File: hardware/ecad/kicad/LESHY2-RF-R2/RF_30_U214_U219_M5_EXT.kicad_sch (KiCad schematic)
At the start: 52 parts, among them J10 Samtec HLE-107-02-G-DV-PE-LC, J11 1125R-SMT-4P, U86 Texas Instruments TPD4E05U06D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, U87 Texas Instruments TPD4E05U06D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, U88 Texas Instruments TPD4E05U06D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, U89 Nexperia 74LVC126APW,118, U90 Nexperia 74LVC126APW,118, U91 TCA4307DGKR, U92 Nexperia 74LVC126APW,118, U93 TPS3808G33DBVR, U94 Texas Instruments TPS259470LR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, U95 Texas Instruments TPD4E05U06D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, U96 Texas Instruments TXS0102DCUR, U97 TPS3808G33DBVR

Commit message: Verify factory-placeable Airband filter
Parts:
- renumbered C236 to C235, C237 to C236, C238 to C237, C239 to C238, C240 to C239, C241 to C240, C242 to C241, C243 to C242, C244 to C243, C245 to C244, C246 to C245, C247 to C246, C248 to C247, C249 to C248
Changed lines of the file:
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@@
 		(on_board yes)
 		(dnp no)
-		(property "Reference" "C236"
+		(property "Reference" "C235"
 			(at 55.88 44.45 0)
 			(show_name no)
@@
 			(project "LESHY2-RF-R2"
 				(path "/ae77990d-9208-5dc0-8562-26b7a6671c82"
-					(reference "C236")
+					(reference "C235")
 					(unit 1)
 				)
@@
 		(on_board yes)
 		(dnp no)
-		(property "Reference" "C237"
+		(property "Reference" "C236"
 			(at 147.32 44.45 0)
 			(show_name no)
@@
 			(project "LESHY2-RF-R2"
 				(path "/ae77990d-9208-5dc0-8562-26b7a6671c82"
-					(reference "C237")
+					(reference "C236")
 					(unit 1)
 				)
@@
 		(on_board yes)
 		(dnp no)
-		(property "Reference" "C238"
+		(property "Reference" "C237"
 			(at 238.76 44.45 0)
 			(show_name no)
@@
 			(project "LESHY2-RF-R2"
 				(path "/ae77990d-9208-5dc0-8562-26b7a6671c82"
-					(reference "C238")
+					(reference "C237")
 					(unit 1)
 				)
@@
 		(on_board yes)
 		(dnp no)
-		(property "Reference" "C239"
+		(property "Reference" "C238"
 			(at 330.20 44.45 0)
 			(show_name no)
@@
 			(project "LESHY2-RF-R2"
 				(path "/ae77990d-9208-5dc0-8562-26b7a6671c82"
-					(reference "C239")
+					(reference "C238")
 					(unit 1)
 				)
@@
 		(on_board yes)
 		(dnp no)
-		(property "Reference" "C240"
+		(property "Reference" "C239"
 			(at 421.64 44.45 0)
 			(show_name no)
@@
 			(project "LESHY2-RF-R2"
 				(path "/ae77990d-9208-5dc0-8562-26b7a6671c82"
-					(reference "C240")
+					(reference "C239")
 					(unit 1)
 				)
@@
 		(on_board yes)
 		(dnp no)
-		(property "Reference" "C241"
+		(property "Reference" "C240"
 			(at 513.08 44.45 0)
 			(show_name no)
@@
 			(project "LESHY2-RF-R2"
 				(path "/ae77990d-9208-5dc0-8562-26b7a6671c82"
-					(reference "C241")
+					(reference "C240")
 					(unit 1)
 				)
@@
 		(on_board yes)
 		(dnp no)
-		(property "Reference" "C242"
+		(property "Reference" "C241"
 			(at 604.52 44.45 0)
 			(show_name no)
@@
 			(project "LESHY2-RF-R2"
 				(path "/ae77990d-9208-5dc0-8562-26b7a6671c82"
-					(reference "C242")
+					(reference "C241")
 					(unit 1)
 				)
@@
 		(on_board yes)
 		(dnp no)
-		(property "Reference" "C243"
+		(property "Reference" "C242"
 			(at 695.96 44.45 0)
 			(show_name no)
@@
 			(project "LESHY2-RF-R2"
 				(path "/ae77990d-9208-5dc0-8562-26b7a6671c82"
-					(reference "C243")
+					(reference "C242")
 					(unit 1)
 				)
@@
 		(on_board yes)
 		(dnp no)
-		(property "Reference" "C244"
+		(property "Reference" "C243"
 			(at 787.40 44.45 0)
 			(show_name no)
@@
 			(project "LESHY2-RF-R2"
 				(path "/ae77990d-9208-5dc0-8562-26b7a6671c82"
-					(reference "C244")
+					(reference "C243")
 					(unit 1)
 				)
@@
 		(on_board yes)
 		(dnp no)
-		(property "Reference" "C245"
+		(property "Reference" "C244"
 			(at 878.84 44.45 0)
 			(show_name no)
@@
 			(project "LESHY2-RF-R2"
 				(path "/ae77990d-9208-5dc0-8562-26b7a6671c82"
-					(reference "C245")
+					(reference "C244")
 					(unit 1)
 				)
@@
 		(on_board yes)
 		(dnp no)
-		(property "Reference" "C246"
+		(property "Reference" "C245"
 			(at 970.28 44.45 0)
 			(show_name no)
@@
 			(project "LESHY2-RF-R2"
 				(path "/ae77990d-9208-5dc0-8562-26b7a6671c82"
-					(reference "C246")
+					(reference "C245")
 					(unit 1)
 				)
@@
 		(on_board yes)
 		(dnp no)
-		(property "Reference" "C247"
+		(property "Reference" "C246"
 			(at 1061.72 44.45 0)
 			(show_name no)
@@
 			(project "LESHY2-RF-R2"
 				(path "/ae77990d-9208-5dc0-8562-26b7a6671c82"
-					(reference "C247")
+					(reference "C246")
 					(unit 1)
 				)
@@
 		(on_board yes)
 		(dnp no)
-		(property "Reference" "C248"
+		(property "Reference" "C247"
 			(at 55.88 80.01 0)
 			(show_name no)
@@
 			(project "LESHY2-RF-R2"
 				(path "/ae77990d-9208-5dc0-8562-26b7a6671c82"
-					(reference "C248")
+					(reference "C247")
 					(unit 1)
 				)
@@
 		(on_board yes)
 		(dnp no)
-		(property "Reference" "C249"
+		(property "Reference" "C248"
 			(at 147.32 80.01 0)
 			(show_name no)
@@
 			(project "LESHY2-RF-R2"
 				(path "/ae77990d-9208-5dc0-8562-26b7a6671c82"
-					(reference "C249")
-					(unit 1)
-				)
+					(reference "C248")
+					(unit 1)
+				)

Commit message: Complete current R2 schematic and sourcing revalidation
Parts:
- removed R214: Panasonic ERJ-2RKF22R0X, Resistor_SMD:R_0402_1005Metric, symbol Leshy2_R2:panasonic_erj_2rkf22r0x
- added C246, C248, C249: Yageo CC0402KRX7R9BB104, Capacitor_SMD:C_0402_1005Metric, symbol Leshy2_R2:yageo_cc0402krx7r9bb104
- added C247: Murata GRM155R71H103KA88D, Capacitor_SMD:C_0402_1005Metric, symbol Leshy2_R2:murata_grm155r71h103ka88d
- added L32: LESHY2-NFC-PICKUP-LOOP-R2, Leshy2_R2:NFC_Pickup_Loop_R2, symbol Leshy2_R2:leshy2_nfc_pickup_loop_r2
- added R226, R232: 0402WGF1003TCE, Resistor_SMD:R_0402_1005Metric, symbol Leshy2_R2:uniroyal_0402wgf1003tce
- added R227: 0402WGF1004TCE, Resistor_SMD:R_0402_1005Metric, symbol Leshy2_R2:uniroyal_0402wgf1004tce
- added R228, R229: 0402WGF1001TCE, Resistor_SMD:R_0402_1005Metric, symbol Leshy2_R2:uniroyal_0402wgf1001tce
- added R230, R231, R233, R234: 0402WGF1002TCE, Resistor_SMD:R_0402_1005Metric, symbol Leshy2_R2:uniroyal_0402wgf1002tce
- added U95, U96: BAT54S,215, Package_TO_SOT_SMD:SOT-23, symbol Leshy2_R2:nexperia_bat54s_215
- added U97: LMV331IDBVR, Package_TO_SOT_SMD:SOT-23-5, symbol Leshy2_R2:ti_lmv331_idbvr
- added U98: Texas Instruments SN74LVC1G06DCKR, Package_TO_SOT_SMD:Texas_R-PDSO-G5_DCK-5, symbol Leshy2_R2:ti_sn74lvc1g06_dckr
- added U99: SN74CBTLV1G125DCKR, Package_TO_SOT_SMD:Texas_R-PDSO-G5_DCK-5, symbol Leshy2_R2:ti_sn74cbtlv1g125_dckr
- renumbered C235 to C240, C236 to C241, C237 to C242, C238 to C243, C239 to C244, C240 to C245, C241 to C250, C242 to C251, C243 to C252, C244 to C253, C245 to C254, C246 to C255, C247 to C256, C248 to C257, R211 to R212, R212 to R213, R213 to R214, R226 to R235, R227 to R236, R228 to R237, R229 to R238, R230 to R239, R231 to R240, R232 to R241, R233 to R242, R234 to R243, U94 to U100, U95 to U101, U96 to U102, U97 to U103, U86 to U87, U87 to U88, U88 to U89, U89 to U90, U90 to U91, U91 to U92, U92 to U93, U93 to U94
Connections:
- net 3V3_MAIN: now also C249.1 (END_1), U99.5 (VCC)
- net AON_SAFE_3V3: now also C246.1 (END_1), C248.1 (END_1), R230.1 (END_1), R232.1 (END_1), R234.1 (END_1), U97.5 (VCC), U98.5 (VCC)
- net POWER_GROUND: now also U93.1 (1OE), U93.2 (1A), C249.2 (END_2), U99.3 (GND)
- net SAFETY_GROUND: now also C246.2 (END_2), C247.2 (END_2), C248.2 (END_2), R226.2 (END_2), R231.2 (END_2), R233.2 (END_2), U95.1 (A1), U96.1 (A1), U97.2 (GND), U98.3 (GND)
- net U214_BUSY_CONNECTOR: now also U99.2 (A); no longer U93.2 (1A)
- net U214_READY: now also R233.1 (END_1), U98.2 (A); no longer U93.1 (1OE)
- net U214_BUSY_BUFFERED: no longer names the net of U93.3 (1Y)
- new net CAP_PIN10_HOST: U99.4 (B)
- new net EV_N9_U219_NFC: R227.1 (END_1), R230.2 (END_2), U97.4 (OUT)
- new net NFC_BRIDGE_AC_N: R228.2 (END_2), U96.3 (K1_A2)
- new net NFC_BRIDGE_AC_P: R229.2 (END_2), U95.3 (K1_A2)
- new net NFC_FIELD_ENV: C247.1 (END_1), R226.1 (END_1), U95.2 (K2), U96.2 (K2), U97.3 (IN_N)
- new net NFC_FIELD_THRESHOLD: R227.2 (END_2), R231.1 (END_1), R232.2 (END_2), U97.1 (IN_P)
- new net NFC_PICKUP_N: L32.2 (END_N), R228.1 (END_1)
- new net NFC_PICKUP_P: L32.1 (END_P), R229.1 (END_1)
- new net U219_PIN10_OE_N: R234.2 (END_2), U98.4 (Y), U99.1 (OE_N)
- no-connect marks 22 -> 24
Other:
- moved on the sheet: C250, C251, C252, C253, C254, C255, C256, C257, J10, J11, R212, R213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

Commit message: Canonicalize physical ground anchors
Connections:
- net SAFETY_GROUND is gone; now on net POWER_GROUND: C244.2 (END_2), C245.2 (END_2), C246.2 (END_2), C247.2 (END_2), C248.2 (END_2), C256.2 (END_2), C257.2 (END_2), R224.2 (END_2), R226.2 (END_2), R231.2 (END_2), R233.2 (END_2), R242.2 (END_2), U103.2 (GND), U94.2 (GND), U95.1 (A1), U96.1 (A1), U97.2 (GND), U98.3 (GND)
- net U214_ESD_GROUND is gone; now on net POWER_GROUND: U87.3 (GND_3), U87.8 (GND_8), U88.3 (GND_3), U88.8 (GND_8), U89.3 (GND_3), U89.8 (GND_8)
- net U214_UNUSED_A_LOW is gone; now on net POWER_GROUND: U91.12 (4A), U91.5 (2A), U91.9 (3A)
- net U214_UNUSED_OE_LOW is gone; now on net POWER_GROUND: U91.10 (3OE), U91.13 (4OE), U91.4 (2OE)
- net UNIT_ESD_GROUND is gone; now on net POWER_GROUND: U101.3 (GND_3), U101.8 (GND_8)
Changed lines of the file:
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@@
 		(effects (font (size 1.27 1.27)))
 	)
-	(hierarchical_label "SAFETY_GROUND"
-		(shape bidirectional)
+	(label "POWER_GROUND"
 		(at 441.96 50.80 180)
 		(effects (font (size 1.27 1.27)) (justify right bottom))
@@
 		(effects (font (size 1.27 1.27)))
 	)
-	(label "SAFETY_GROUND"
+	(label "POWER_GROUND"
 		(at 533.40 50.80 180)
 		(effects (font (size 1.27 1.27)) (justify right bottom))
@@
 		(effects (font (size 1.27 1.27)))
 	)
-	(label "SAFETY_GROUND"
+	(label "POWER_GROUND"
 		(at 624.84 50.80 180)
 		(effects (font (size 1.27 1.27)) (justify right bottom))
@@
 		(effects (font (size 1.27 1.27)))
 	)
-	(label "SAFETY_GROUND"
+	(label "POWER_GROUND"
 		(at 716.28 50.80 180)
 		(effects (font (size 1.27 1.27)) (justify right bottom))
@@
 		(effects (font (size 1.27 1.27)))
 	)
-	(label "SAFETY_GROUND"
+	(label "POWER_GROUND"
 		(at 807.72 50.80 180)
 		(effects (font (size 1.27 1.27)) (justify right bottom))
@@
 		(effects (font (size 1.27 1.27)))
 	)
-	(label "SAFETY_GROUND"
+	(label "POWER_GROUND"
 		(at 441.96 86.36 180)
 		(effects (font (size 1.27 1.27)) (justify right bottom))
@@
 		(effects (font (size 1.27 1.27)))
 	)
-	(label "SAFETY_GROUND"
+	(label "POWER_GROUND"
 		(at 533.40 86.36 180)
 		(effects (font (size 1.27 1.27)) (justify right bottom))
@@
 		(effects (font (size 1.27 1.27)))
 	)
-	(label "SAFETY_GROUND"
+	(label "POWER_GROUND"
 		(at 990.60 121.92 180)
 		(effects (font (size 1.27 1.27)) (justify right bottom))
@@
 		(effects (font (size 1.27 1.27)))
 	)
-	(label "SAFETY_GROUND"
+	(label "POWER_GROUND"
 		(at 624.84 129.54 180)
 		(effects (font (size 1.27 1.27)) (justify right bottom))
@@
 		(effects (font (size 1.27 1.27)))
 	)
-	(label "SAFETY_GROUND"
+	(label "POWER_GROUND"
 		(at 441.96 157.48 180)
 		(effects (font (size 1.27 1.27)) (justify right bottom))
@@
 		(effects (font (size 1.27 1.27)))
 	)
-	(label "SAFETY_GROUND"
+	(label "POWER_GROUND"
 		(at 716.28 157.48 180)
 		(effects (font (size 1.27 1.27)) (justify right bottom))
@@
 		(effects (font (size 1.27 1.27)))
 	)
-	(label "SAFETY_GROUND"
+	(label "POWER_GROUND"
 		(at 350.52 193.04 180)
 		(effects (font (size 1.27 1.27)) (justify right bottom))
@@
 		(effects (font (size 1.27 1.27)))
 	)
-	(label "U214_ESD_GROUND"
+	(label "POWER_GROUND"
 		(at 492.76 195.58 0)
 		(effects (font (size 1.27 1.27)))
@@
 	(no_connect (at 533.40 193.04)
 	)
-	(label "U214_ESD_GROUND"
+	(label "POWER_GROUND"
 		(at 533.40 195.58 180)
 		(effects (font (size 1.27 1.27)) (justify right bottom))
@@
 		(effects (font (size 1.27 1.27)))
 	)
-	(label "U214_ESD_GROUND"
+	(label "POWER_GROUND"
 		(at 675.64 195.58 0)
 		(effects (font (size 1.27 1.27)))
@@
 	(no_connect (at 716.28 193.04)
 	)
-	(label "U214_ESD_GROUND"
+	(label "POWER_GROUND"
 		(at 716.28 195.58 180)
 		(effects (font (size 1.27 1.27)) (justify right bottom))
@@
 		(effects (font (size 1.27 1.27)))
 	)
-	(label "U214_ESD_GROUND"
+	(label "POWER_GROUND"
 		(at 767.08 195.58 0)
 		(effects (font (size 1.27 1.27)))
@@
 	(no_connect (at 807.72 193.04)
 	)
-	(label "U214_ESD_GROUND"
+	(label "POWER_GROUND"
 		(at 807.72 195.58 180)
 		(effects (font (size 1.27 1.27)) (justify right bottom))
@@
 		(effects (font (size 1.27 1.27)))
 	)
-	(label "U214_UNUSED_OE_LOW"
+	(label "POWER_GROUND"
 		(at 949.96 198.12 0)
 		(effects (font (size 1.27 1.27)))
 	)
-	(label "U214_UNUSED_A_LOW"
+	(label "POWER_GROUND"
 		(at 949.96 200.66 0)
 		(effects (font (size 1.27 1.27)))
@@
 	(no_connect (at 990.60 190.50)
 	)
-	(label "U214_UNUSED_A_LOW"
+	(label "POWER_GROUND"
 		(at 990.60 193.04 180)
 		(effects (font (size 1.27 1.27)) (justify right bottom))
 	)
-	(label "U214_UNUSED_OE_LOW"
+	(label "POWER_GROUND"
 		(at 990.60 195.58 180)
 		(effects (font (size 1.27 1.27)) (justify right bottom))
@@
 	(no_connect (at 990.60 198.12)
 	)
-	(label "U214_UNUSED_A_LOW"
+	(label "POWER_GROUND"
 		(at 990.60 200.66 180)
 		(effects (font (size 1.27 1.27)) (justify right bottom))
 	)
-	(label "U214_UNUSED_OE_LOW"
+	(label "POWER_GROUND"
 		(at 990.60 203.20 180)
 		(effects (font (size 1.27 1.27)) (justify right bottom))
@@
 		(effects (font (size 1.27 1.27)))
 	)
-	(label "SAFETY_GROUND"
+	(label "POWER_GROUND"
 		(at 35.56 229.87 0)
 		(effects (font (size 1.27 1.27)))
@@
 		)
 	)
-	(label "SAFETY_GROUND"
+	(label "POWER_GROUND"
 		(at 127.00 228.60 0)
 		(effects (font (size 1.27 1.27)))
@@
 		)
 	)
-	(label "SAFETY_GROUND"
+	(label "POWER_GROUND"
 		(at 218.44 228.60 0)
 		(effects (font (size 1.27 1.27)))
@@
 		(effects (font (size 1.27 1.27)))
 	)
-	(label "SAFETY_GROUND"
+	(label "POWER_GROUND"
 		(at 309.88 229.87 0)
 		(effects (font (size 1.27 1.27)))
@@
 		(effects (font (size 1.27 1.27)))
 	)
-	(label "SAFETY_GROUND"
+	(label "POWER_GROUND"
 		(at 401.32 232.41 0)
 		(effects (font (size 1.27 1.27)))
@@
 		(effects (font (size 1.27 1.27)))
 	)
-	(label "UNIT_ESD_GROUND"
+	(label "POWER_GROUND"
 		(at 675.64 233.68 0)
 		(effects (font (size 1.27 1.27)))
@@
 	(no_connect (at 716.28 231.14)
 	)
-	(label "UNIT_ESD_GROUND"
+	(label "POWER_GROUND"
 		(at 716.28 233.68 180)
 		(effects (font (size 1.27 1.27)) (justify right bottom))
@@
 		(effects (font (size 1.27 1.27)))
 	)
-	(label "SAFETY_GROUND"
+	(label "POWER_GROUND"
 		(at 858.52 237.49 0)
 		(effects (font (size 1.27 1.27)))

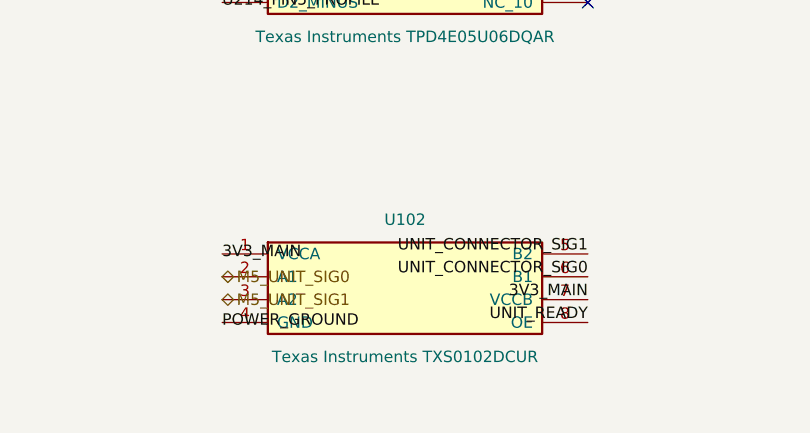
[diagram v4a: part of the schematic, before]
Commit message: Fix exact pin maps and RP flash power; add typed electrical review
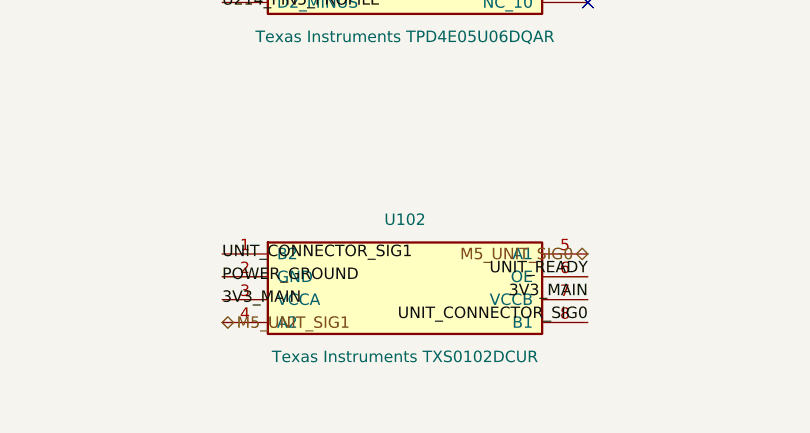
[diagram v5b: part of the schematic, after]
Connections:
- net 3V3_MAIN: now also U102.3 (VCCA); no longer U102.1 (VCCA)
- net M5_UNIT_SIG0: now also U102.5 (A1); no longer U102.2 (A1)
- net M5_UNIT_SIG1: now also U102.4 (A2); no longer U102.3 (A2)
- net POWER_GROUND: now also U102.2 (GND); no longer U102.4 (GND)
- net UNIT_CONNECTOR_SIG0: now also U102.8 (B1); no longer U102.6 (B1)
- net UNIT_CONNECTOR_SIG1: now also U102.1 (B2); no longer U102.5 (B2)
- net UNIT_READY: now also U102.6 (OE); no longer U102.8 (OE)
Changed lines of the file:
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@@
 		)
 	)
+	(label "UNIT_CONNECTOR_SIG1"
+		(at 767.08 228.60 0)
+		(effects (font (size 1.27 1.27)))
+	)
+	(label "POWER_GROUND"
+		(at 767.08 231.14 0)
+		(effects (font (size 1.27 1.27)))
+	)
 	(label "3V3_MAIN"
-		(at 767.08 228.60 0)
+		(at 767.08 233.68 0)
+		(effects (font (size 1.27 1.27)))
+	)
+	(hierarchical_label "M5_UNIT_SIG1"
+		(shape bidirectional)
+		(at 767.08 236.22 0)
 		(effects (font (size 1.27 1.27)))
 	)
 	(hierarchical_label "M5_UNIT_SIG0"
 		(shape bidirectional)
-		(at 767.08 231.14 0)
-		(effects (font (size 1.27 1.27)))
-	)
-	(hierarchical_label "M5_UNIT_SIG1"
-		(shape bidirectional)
-		(at 767.08 233.68 0)
-		(effects (font (size 1.27 1.27)))
-	)
-	(label "POWER_GROUND"
-		(at 767.08 236.22 0)
-		(effects (font (size 1.27 1.27)))
-	)
-	(label "UNIT_CONNECTOR_SIG1"
 		(at 807.72 228.60 180)
 		(effects (font (size 1.27 1.27)) (justify right bottom))
 	)
-	(label "UNIT_CONNECTOR_SIG0"
+	(label "UNIT_READY"
 		(at 807.72 231.14 180)
 		(effects (font (size 1.27 1.27)) (justify right bottom))
@@
 		(effects (font (size 1.27 1.27)) (justify right bottom))
 	)
-	(label "UNIT_READY"
+	(label "UNIT_CONNECTOR_SIG0"
 		(at 807.72 236.22 180)
 		(effects (font (size 1.27 1.27)) (justify right bottom))
